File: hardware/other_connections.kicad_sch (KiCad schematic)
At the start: 46 parts, among them J10 USB_B_Micro, J11 USB_B_Micro, J12 USB_B_Micro, J13 Conn_02x05_Odd_Even, J14 Conn_02x05_Odd_Even, J15 Conn_01x02, J9 USB_B_Micro, U12 CH330N, U13 CH330N

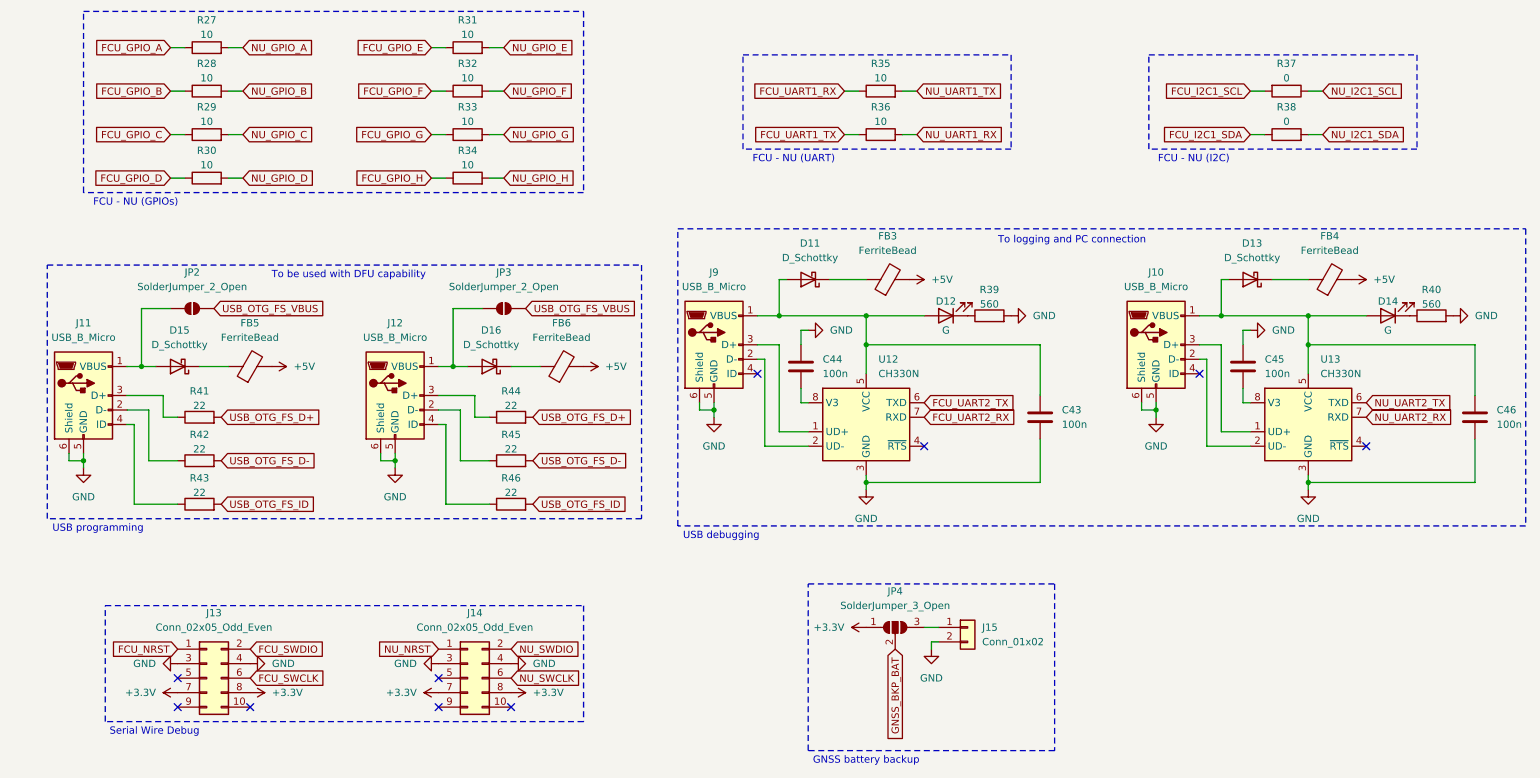
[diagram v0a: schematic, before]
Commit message: schematic and BOM done
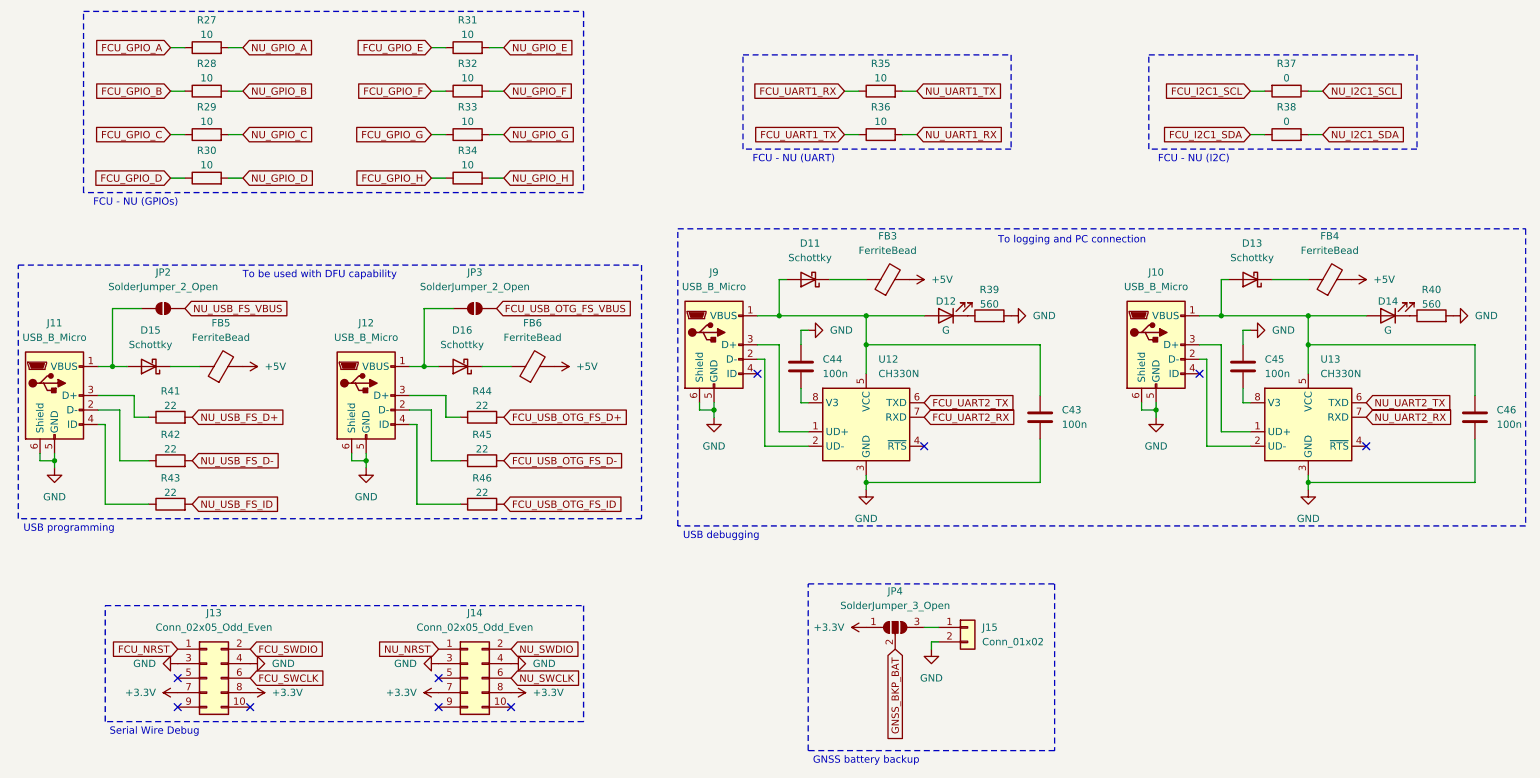
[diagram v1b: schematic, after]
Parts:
- C43, C44, C45, C46: footprint (none) -> Capacitor_SMD:C_0603_1608Metric
- D11, D13, D15, D16: value D_Schottky -> Schottky; footprint (none) -> airplane:SOD2713X115N
- D12, D14: footprint (none) -> LED_SMD:LED_0603_1608Metric
- FB3, FB4, FB5, FB6: footprint (none) -> Inductor_SMD:L_0603_1608Metric
- J10, J11, J12, J9: footprint (none) -> Connector_USB:USB_Micro-B_Molex_47346-0001; Manufacturer Part Number (none) -> 0473461001
- J13, J14: footprint (none) -> airplane:JST_PHD_B10B-PHDSS_2x05_P2.00mm_Vertical; Manufacturer Part Number (none) -> B10B-PHDSS
- J15: footprint (none) -> Connector_JST:JST_PH_S2B-PH-K_1x02_P2.00mm_Horizontal; Manufacturer Part Number (none) -> S2B-PH-K-S
- JP2, JP3: footprint (none) -> Jumper:SolderJumper-2_P1.3mm_Open_RoundedPad1.0x1.5mm
- JP4: footprint (none) -> Jumper:SolderJumper-3_P1.3mm_Open_RoundedPad1.0x1.5mm
- R27, R28, R29, R30, R31, R32, R33, R34, R35, R36, R37, R38, R39, R40, R41, R42, R43, R44, R45, R46: footprint (none) -> Resistor_SMD:R_0603_1608Metric
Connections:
- net USB_OTG_FS_D+ renamed FCU_USB_OTG_FS_D+
- net FCU_USB_OTG_FS_D+: no longer R41.2
- net USB_OTG_FS_D- renamed FCU_USB_OTG_FS_D-
- net FCU_USB_OTG_FS_D-: no longer R42.2
- net USB_OTG_FS_ID renamed FCU_USB_OTG_FS_ID
- net FCU_USB_OTG_FS_ID: no longer R43.2
- net USB_OTG_FS_VBUS renamed FCU_USB_OTG_FS_VBUS
- net FCU_USB_OTG_FS_VBUS: no longer JP2.2 (B)
- new net NU_USB_FS_D+: R41.2
- new net NU_USB_FS_D-: R42.2
- new net NU_USB_FS_ID: R43.2
- new net NU_USB_FS_VBUS: JP2.2 (B)
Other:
- moved on the sheet: D15, D16, FB5, FB6, J11, J12, JP2, JP3, R41, R42, R43, R44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
